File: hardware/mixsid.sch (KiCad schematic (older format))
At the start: 72 parts, among them P1 INPUT, P2 CONTROL, P3 RAW, P4 SOCKET LEFT, P5 OUTPUT, P6 SOCKET RIGHT, Q1 BC547, Q2 BC547, U1 GAL16V8, U2 SID2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

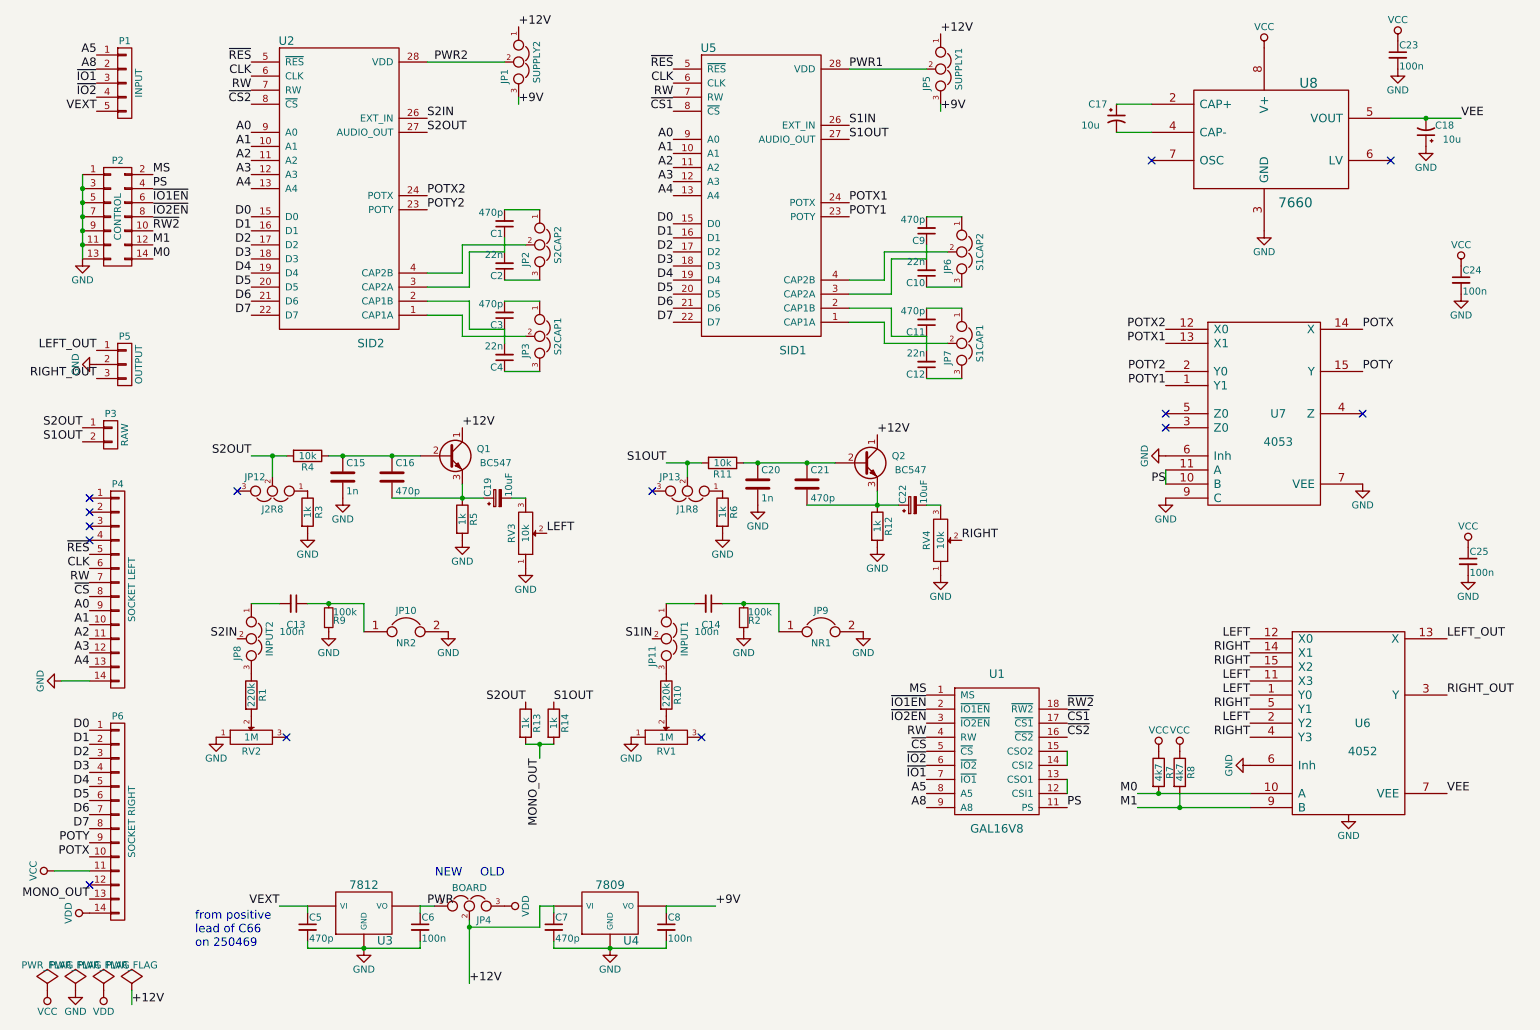
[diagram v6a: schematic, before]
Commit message: Hardware: Added bypass caps at SID VDD supplies
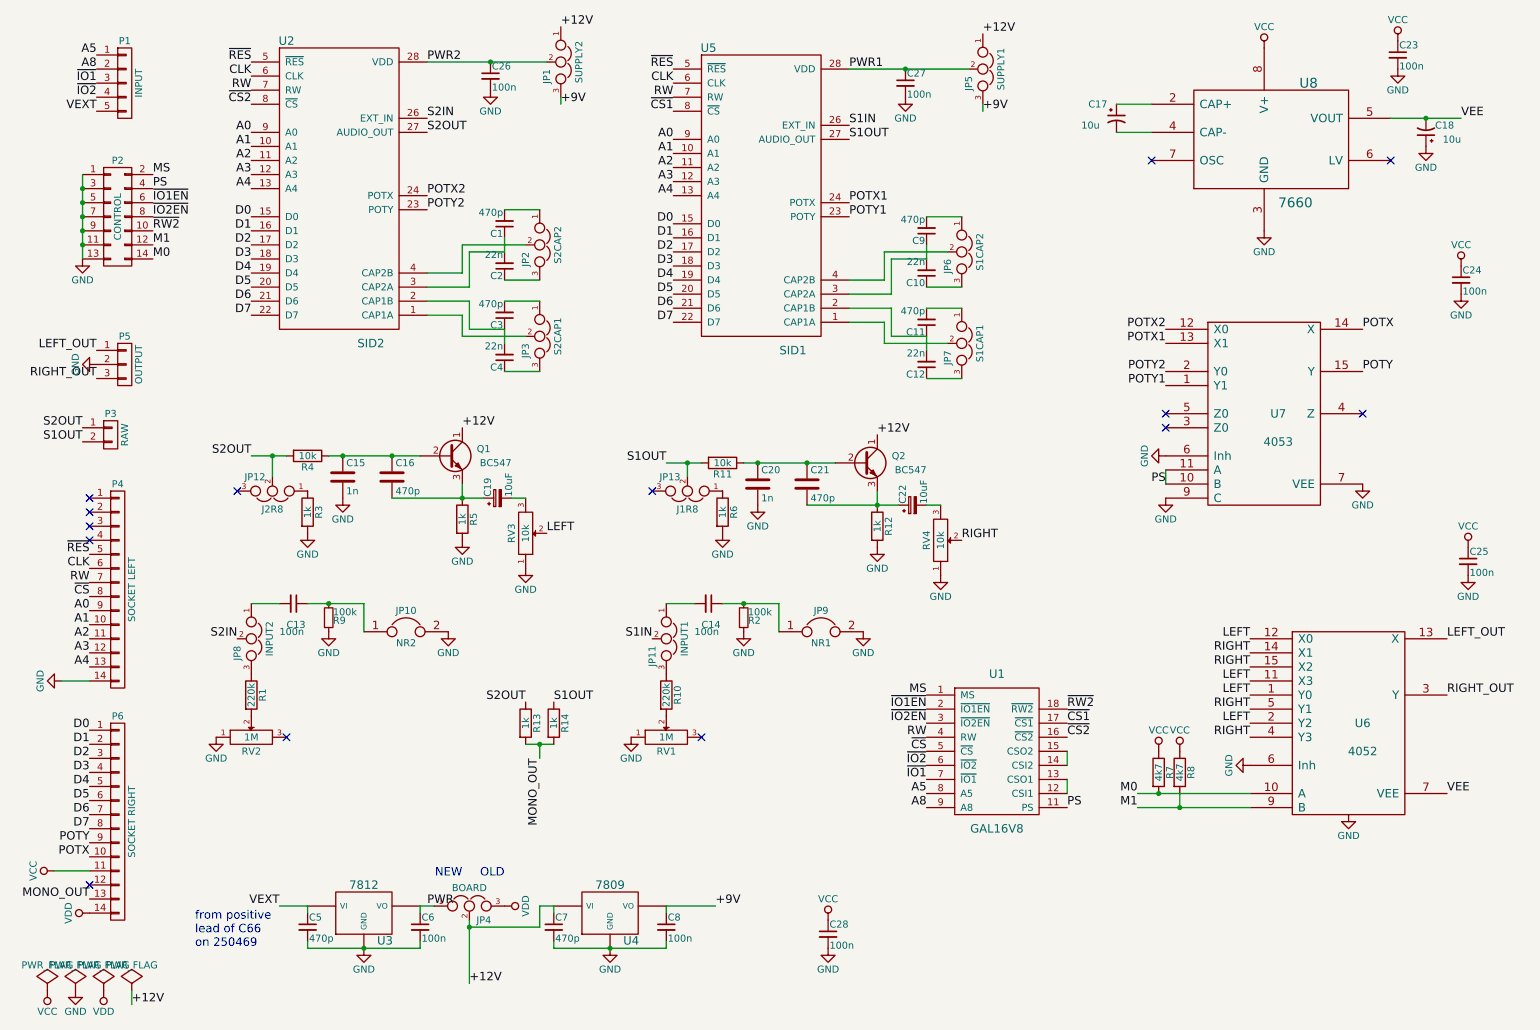
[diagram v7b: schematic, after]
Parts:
- added C26, C27, C28: 100n, Pinheaders:C_Disc_D3_P2.5, symbol C_Small
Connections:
- net GND: now also C26.2, C27.2, C28.2
- net PWR1: now also C27.1
- net PWR2: now also C26.1
- net VCC: now also C28.1
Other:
- moved on the sheet: JP1, JP5
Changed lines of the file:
@@
 L JUMPER3 JP1
 U 1 1 56D89887
-P 4050 950
-F 0 "JP1" H 4100 850 50  0000 L CNN
-F 1 "SUPPLY2" H 4050 1050 50  0000 C BNN
-F 2 "Pinheaders:Pin_Header_Straight_1x03_Pitch2.00mm" H 4050 950 60  0001 C CNN
-F 3 "" H 4050 950 60  0000 C CNN
-	1    4050 950
+P 4350 950
+F 0 "JP1" H 4400 850 50  0000 L CNN
+F 1 "SUPPLY2" H 4350 1050 50  0000 C BNN
+F 2 "Pinheaders:Pin_Header_Straight_1x03_Pitch2.00mm" H 4350 950 60  0001 C CNN
+F 3 "" H 4350 950 60  0000 C CNN
+	1    4350 950
 	0    1    1    0
 $EndComp
-Text Label 4050 700  0    60   ~ 0
+Text Label 4350 700  0    60   ~ 0
 +12V
-Text Label 4050 1250 0    60   ~ 0
+Text Label 4350 1250 0    60   ~ 0
 +9V
 $Comp
 L JUMPER3 JP5
 U 1 1 56D8AC84
-P 7050 1000
-F 0 "JP5" H 7100 900 50  0000 L CNN
-F 1 "SUPPLY1" H 7050 1100 50  0000 C BNN
-F 2 "Pinheaders:Pin_Header_Straight_1x03_Pitch2.00mm" H 7050 1000 60  0001 C CNN
-F 3 "" H 7050 1000 60  0000 C CNN
-	1    7050 1000
+P 7350 1000
+F 0 "JP5" H 7400 900 50  0000 L CNN
+F 1 "SUPPLY1" H 7350 1100 50  0000 C BNN
+F 2 "Pinheaders:Pin_Header_Straight_1x03_Pitch2.00mm" H 7350 1000 60  0001 C CNN
+F 3 "" H 7350 1000 60  0000 C CNN
+	1    7350 1000
 	0    1    1    0
 $EndComp
-Text Label 7050 750  0    60   ~ 0
+Text Label 7350 750  0    60   ~ 0
 +12V
-Text Label 7050 1300 0    60   ~ 0
+Text Label 7350 1300 0    60   ~ 0
 +9V
 $Comp
@@
 	6650 2800 6400 2800
 Wire Wire Line
-	4050 1200 4050 1250
-Wire Wire Line
-	7050 1250 7050 1300
+	4350 1200 4350 1250
+Wire Wire Line
+	7350 1250 7350 1300
 Wire Wire Line
 	3450 6950 3350 6950
@@
 Wire Wire Line
 	750  6700 1000 6700
-Wire Wire Line
-	6950 1000 6400 1000
-Wire Wire Line
-	3950 950  3400 950
 Wire Wire Line
 	5900 4800 5900 5000
@@
 	1    0    0    -1
 $EndComp
-Text Label 3450 950  0    60   ~ 0
+Text Label 3400 950  0    60   ~ 0
 PWR2
 Text Label 6400 1000 0    60   ~ 0
@@
 Text Label 6600 3600 0    60   ~ 0
 +12V
+$Comp
+L C_Small C26
+U 1 1 5742C306
+P 3850 1050
+F 0 "C26" H 3860 1120 50  0000 L CNN
+F 1 "100n" H 3860 970 50  0000 L CNN
+F 2 "Pinheaders:C_Disc_D3_P2.5" H 3850 1050 60  0001 C CNN
+F 3 "" H 3850 1050 60  0000 C CNN
+	1    3850 1050
+	1    0    0    -1
+$EndComp
+$Comp
+L GND #PWR046
+U 1 1 5742C3ED
+P 3850 1150
+F 0 "#PWR046" H 3850 900 50  0001 C CNN
+F 1 "GND" H 3850 1000 50  0000 C CNN
+F 2 "" H 3850 1150 60  0000 C CNN
+F 3 "" H 3850 1150 60  0000 C CNN
+	1    3850 1150
+	1    0    0    -1
+$EndComp
+Wire Wire Line
+	3400 950  4250 950
+Connection ~ 3850 950
+$Comp
+L C_Small C27
+U 1 1 5742F42C
+P 6800 1100
+F 0 "C27" H 6810 1170 50  0000 L CNN
+F 1 "100n" H 6810 1020 50  0000 L CNN
+F 2 "Pinheaders:C_Disc_D3_P2.5" H 6800 1100 60  0001 C CNN
+F 3 "" H 6800 1100 60  0000 C CNN
+	1    6800 1100
+	1    0    0    -1
+$EndComp
+Wire Wire Line
+	6400 1000 7250 1000
+Connection ~ 6800 1000
+$Comp
+L GND #PWR047
+U 1 1 5742F766
+P 6800 1200
+F 0 "#PWR047" H 6800 950 50  0001 C CNN
+F 1 "GND" H 6800 1050 50  0000 C CNN
+F 2 "" H 6800 1200 60  0000 C CNN
+F 3 "" H 6800 1200 60  0000 C CNN
+	1    6800 1200
+	1    0    0    -1
+$EndComp
+$Comp
+L C_Small C28
+U 1 1 57431743
+P 6250 7150
+F 0 "C28" H 6260 7220 50  0000 L CNN
+F 1 "100n" H 6260 7070 50  0000 L CNN
+F 2 "Pinheaders:C_Disc_D3_P2.5" H 6250 7150 60  0001 C CNN
+F 3 "" H 6250 7150 60  0000 C CNN
+	1    6250 7150
+	1    0    0    -1
+$EndComp
+$Comp
+L VCC #PWR048
+U 1 1 57431749
+P 6250 7050
+F 0 "#PWR048" H 6250 6900 50  0001 C CNN
+F 1 "VCC" H 6250 7200 50  0000 C CNN
+F 2 "" H 6250 7050 60  0000 C CNN
+F 3 "" H 6250 7050 60  0000 C CNN
+	1    6250 7050
+	1    0    0    -1
+$EndComp
+$Comp
+L GND #PWR049
+U 1 1 5743174F
+P 6250 7250
+F 0 "#PWR049" H 6250 7000 50  0001 C CNN
+F 1 "GND" H 6250 7100 50  0000 C CNN
+F 2 "" H 6250 7250 60  0000 C CNN
+F 3 "" H 6250 7250 60  0000 C CNN
+	1    6250 7250
+	1    0    0    -1
+$EndComp
 $EndSCHEMATC

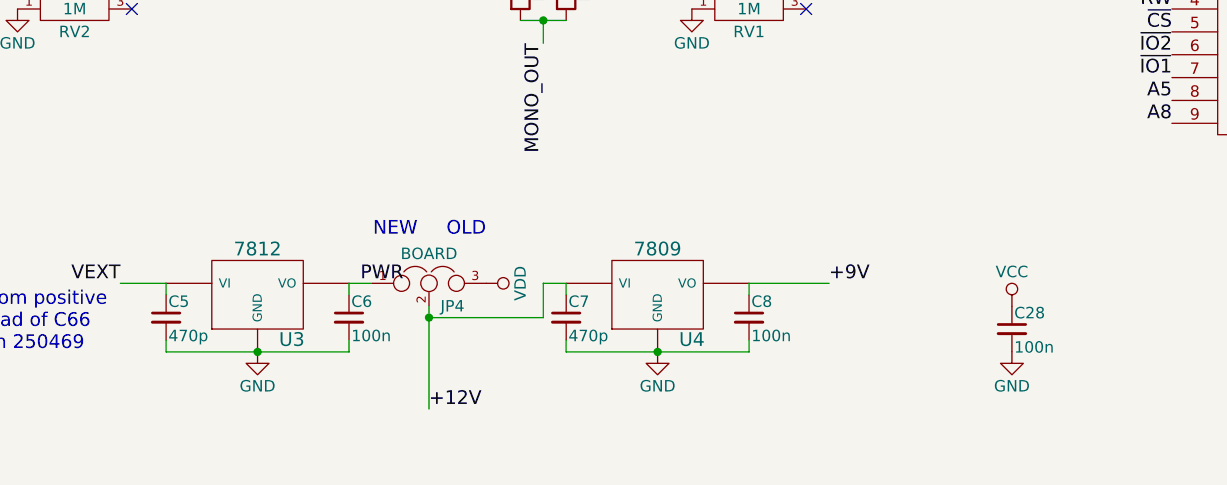
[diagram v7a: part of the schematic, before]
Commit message: Hardware: Added protection diodes to regulators, board height increased
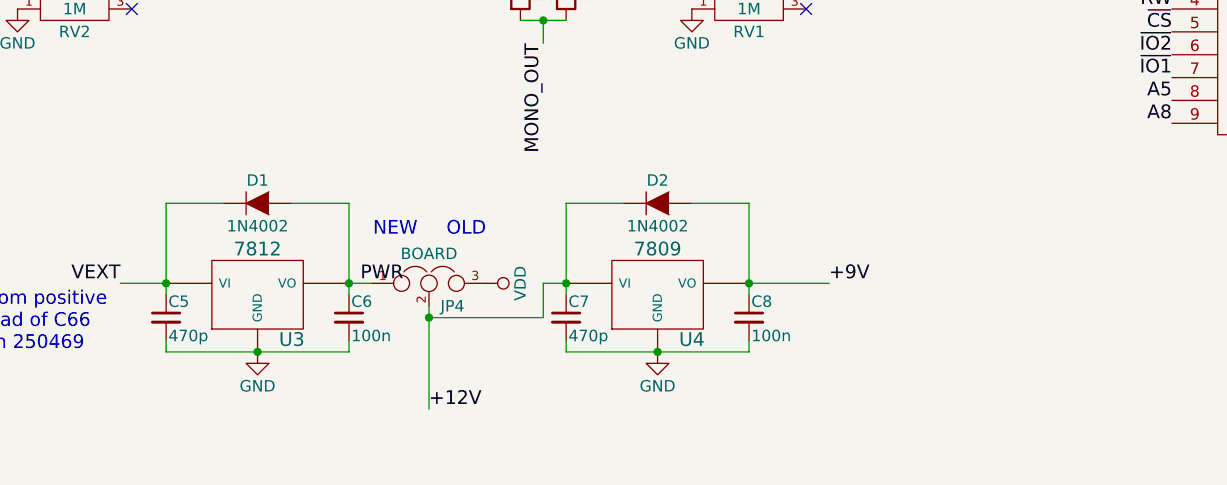
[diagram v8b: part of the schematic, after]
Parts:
- removed C28: 100n, Pinheaders:C_Disc_D3_P2.5, symbol C_Small
- added D1, D2: 1N4002, Discret:DO-41, symbol D
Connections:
- net +12V: now also D2.1 (K)
- net +9V: now also D2.2 (A)
- net PWR: now also D1.2 (A)
- net VEXT: now also D1.1 (K)
